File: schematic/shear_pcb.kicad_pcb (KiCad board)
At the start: 2 copper layers, 53.3 x 66 mm, 3 parts, among them U1 Teensy3.5, U2 AMIS30542, U3 AMIS30542

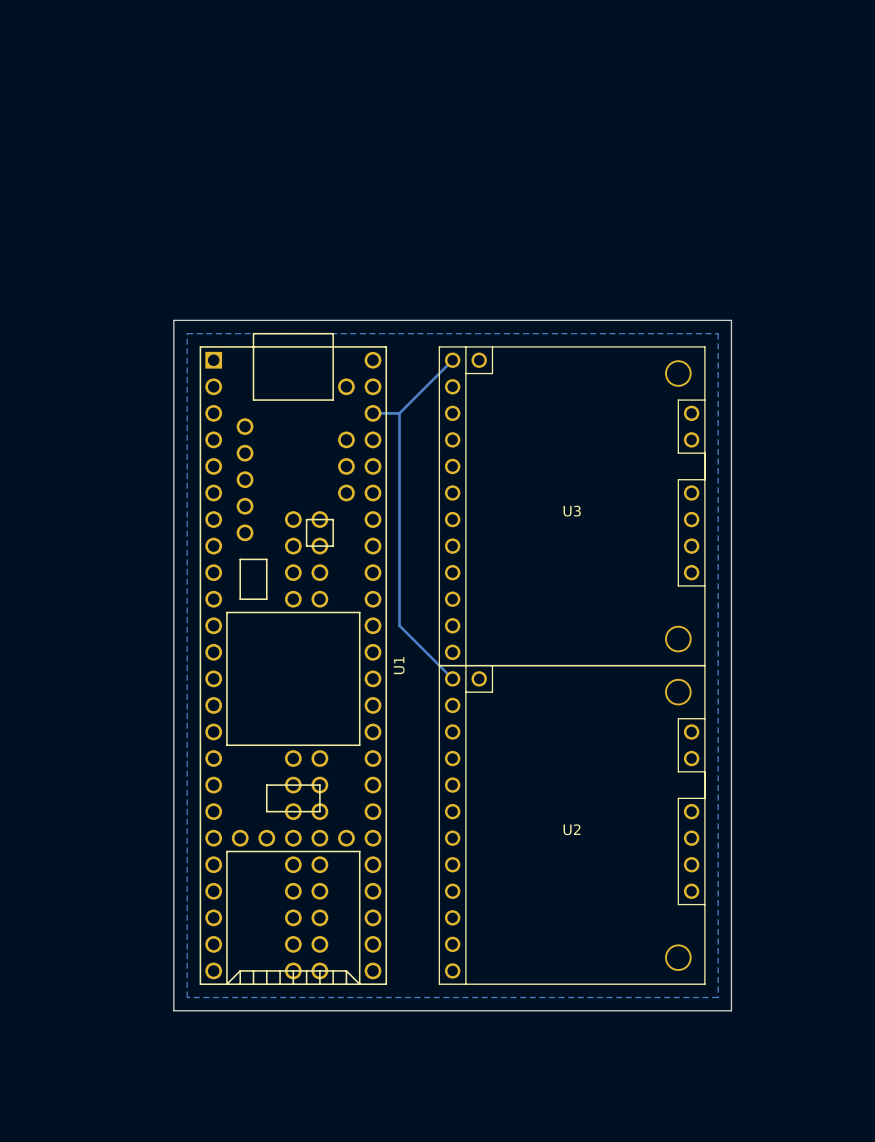
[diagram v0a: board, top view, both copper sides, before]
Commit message: Add connectors and first pcb design
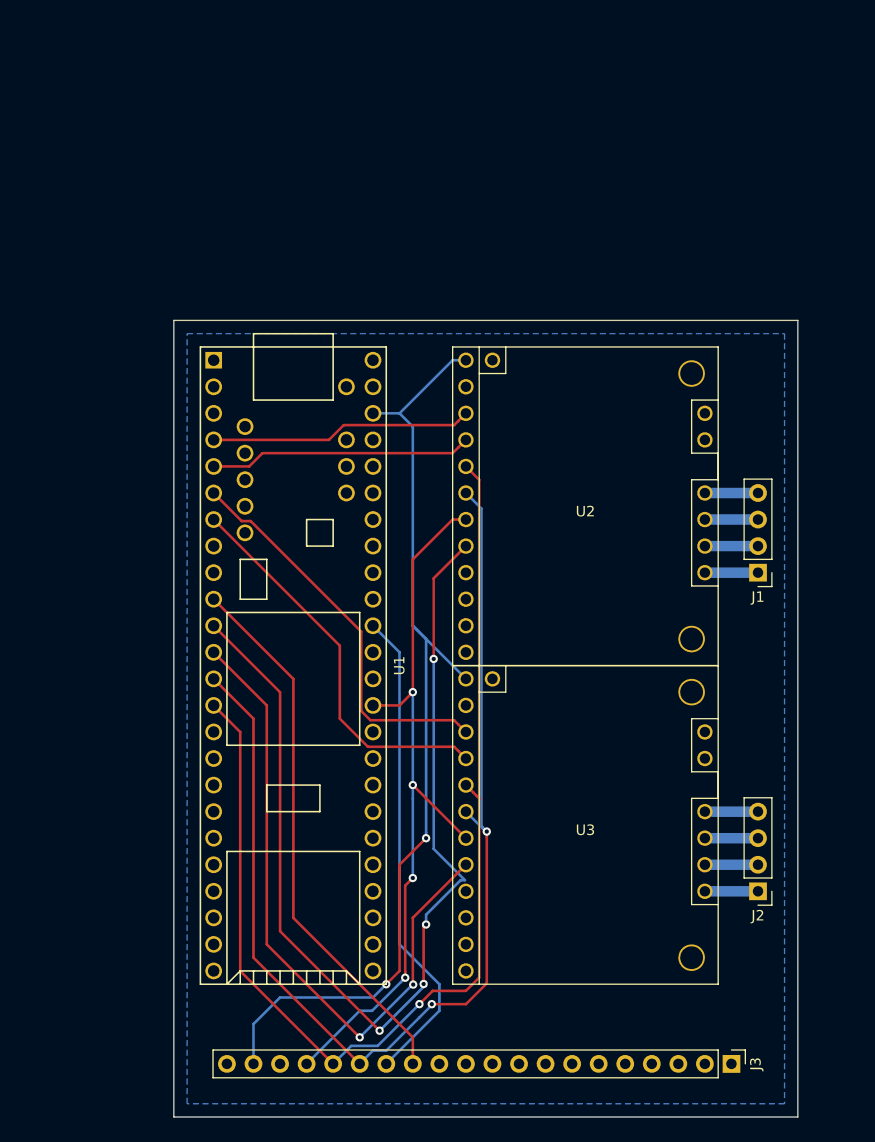
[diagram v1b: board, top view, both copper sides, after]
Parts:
- added J1: MOTOR1, Connector_PinHeader_2.54mm:PinHeader_1x04_P2.54mm_Vertical, F.Cu at (189.2, 97.8)
- added J2: MOTOR2, Connector_PinHeader_2.54mm:PinHeader_1x04_P2.54mm_Vertical, F.Cu at (189.2, 128.3)
- added J3: LCD_CONN, Connector_PinHeader_2.54mm:PinHeader_1x20_P2.54mm_Vertical, F.Cu at (186.7, 144.8)
- moved U2 30.5 mm to (172.7, 91.4)
- moved U3 30.5 mm to (172.7, 121.9)
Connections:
- U1 pad 10: Net-(U1-Pad10) -> D\C
- U1 pad 11: Net-(U1-Pad11) -> CS1
- U1 pad 12: Net-(U1-Pad12) -> CS2
- U1 pad 13: Net-(U1-Pad13) -> MOSI
- U1 pad 14: Net-(U1-Pad14) -> MISO
- U1 pad 4: Net-(U1-Pad4) -> STEP1
- U1 pad 40: Net-(U1-Pad40) -> CLK
- U1 pad 43: Net-(U1-Pad43) -> CS3
- U1 pad 5: Net-(U1-Pad5) -> DIR1
- U1 pad 6: Net-(U1-Pad6) -> STEP2
- U1 pad 7: Net-(U1-Pad7) -> DIR2
- U2 pad 14: GND -> Net-(U2-Pad14)
- U2 pad 15: Net-(U2-Pad15) -> GND
- U2 pad 19: (no net) -> Net-(J1-Pad1)
- U2 pad 4: Net-(U2-Pad4) -> STEP1
- U2 pad 5: Net-(U2-Pad5) -> DIR1
- U2 pad 6: Net-(U2-Pad6) -> MISO
- U2 pad 7: Net-(U2-Pad7) -> MOSI
- U2 pad 8: Net-(U2-Pad8) -> CLK
- U2 pad 9: Net-(U2-Pad9) -> CS1
- U3 pad 14: GND -> Net-(U3-Pad14)
- U3 pad 15: Net-(U3-Pad15) -> GND
- U3 pad 19: (no net) -> Net-(J2-Pad1)
- U3 pad 4: Net-(U3-Pad4) -> STEP2
- U3 pad 5: Net-(U3-Pad5) -> DIR2
- U3 pad 6: Net-(U3-Pad6) -> MISO
- U3 pad 7: Net-(U3-Pad7) -> MOSI
- U3 pad 8: Net-(U3-Pad8) -> CLK
- U3 pad 9: Net-(U3-Pad9) -> CS2
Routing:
- net MOSI: track 0.00 -> 108.5 mm, vias 0 -> 2
- net MISO: track 0.00 -> 107.6 mm, vias 0 -> 1
- net CS1: track 0.00 -> 97.8 mm, vias 0 -> 4
- net CLK: track 0.00 -> 71.3 mm, vias 0 -> 4
- net CS2: track 0.00 -> 63.4 mm, vias 0 -> 2
- net +3V3: track 37.2 -> 93.5 mm, vias 0 -> 2
- net D\C: track 0.00 -> 52.3 mm
- net CS3: track 0.00 -> 46.6 mm
- net STEP2: track 0.00 -> 38.1 mm
- net DIR2: track 0.00 -> 37.7 mm
- net STEP1: track 0.00 -> 25.2 mm
- net DIR1: track 0.00 -> 25.2 mm
- net Net-(J2-Pad4): track 0.00 -> 5.08 mm
- net Net-(J2-Pad3): track 0.00 -> 5.08 mm
- net Net-(J2-Pad2): track 0.00 -> 5.08 mm
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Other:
- board size 53.3 x 66 mm -> 59.7 x 76.2 mm
- net class Motor added: clearance 0.2, trace_width 1, via_dia 0.8, via_drill 0.4

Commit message: Redesign PCB for single-side fabrication
-Add power and endstop connectors
-Add LCD connector
-Reroute SPI and step/dir tracks
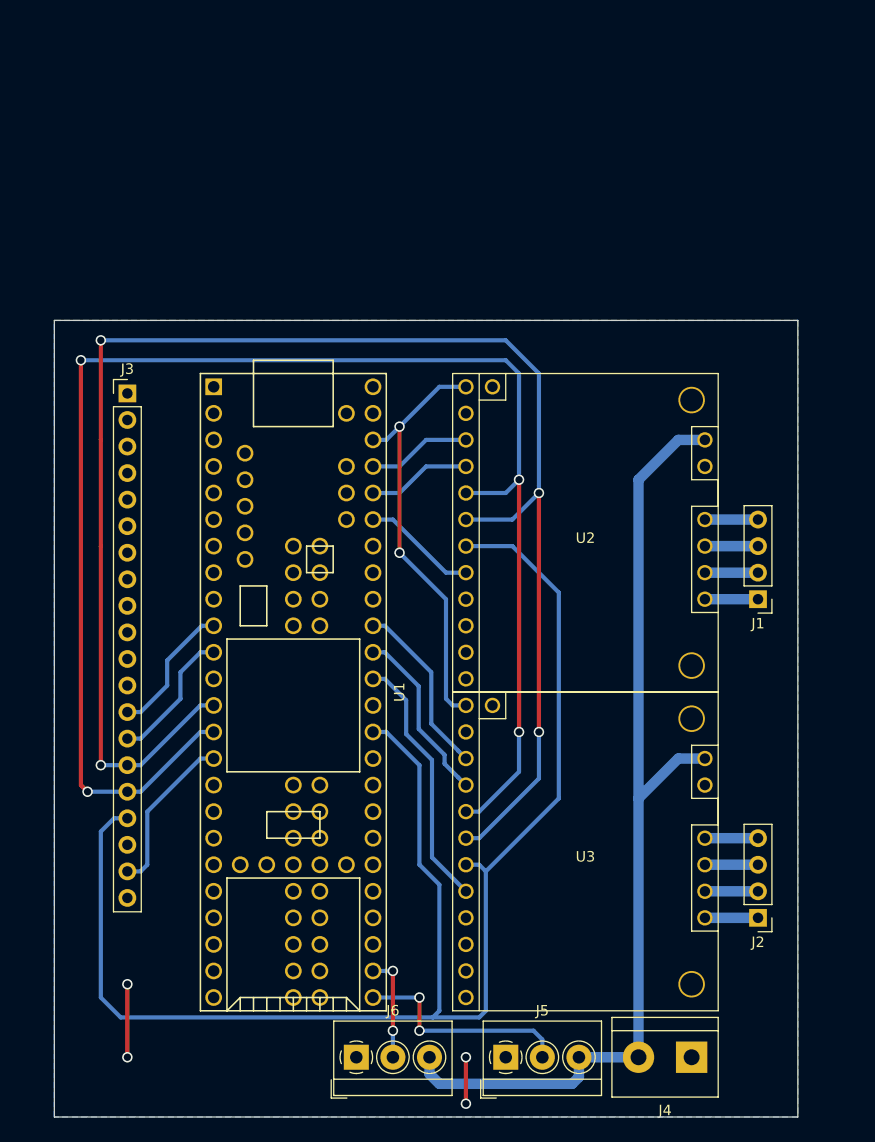
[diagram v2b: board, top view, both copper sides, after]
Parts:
- added J4: VIN, TerminalBlock:TerminalBlock_bornier-2_P5.08mm, F.Cu at (182.9, 144.1)
- added J5: ENDSTOP1, TerminalBlock_4Ucon:TerminalBlock_4Ucon_1x03_P3.50mm_Horizontal, F.Cu at (165.1, 144.1)
- added J6: ENDSTOP2, TerminalBlock_4Ucon:TerminalBlock_4Ucon_1x03_P3.50mm_Horizontal, F.Cu at (150.8, 144.1)
- moved J3 86.3 mm to (128.9, 80.6), turned to 0 degrees
- moved U2 2.54 mm to (172.7, 94.0)
- moved J1 2.54 mm to (189.2, 100.3)
- moved J2 2.54 mm to (189.2, 130.8)
- moved U1 2.54 mm to (144.8, 109.2)
- moved U3 2.54 mm to (172.7, 124.5)
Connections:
- J3 pad 1: Net-(J3-Pad1) -> (no net)
- J3 pad 10: YP -> (no net)
- J3 pad 11: Net-(J3-Pad11) -> (no net)
- J3 pad 12: Net-(J3-Pad12) -> (no net)
- J3 pad 14: CS3 -> CS1
- J3 pad 18: Net-(J3-Pad18) -> (no net)
- J3 pad 2: Net-(J3-Pad2) -> (no net)
- J3 pad 3: Net-(J3-Pad3) -> (no net)
- J3 pad 4: Net-(J3-Pad4) -> (no net)
- J3 pad 5: Net-(J3-Pad5) -> (no net)
- J3 pad 6: Net-(J3-Pad6) -> (no net)
- J3 pad 7: XM -> (no net)
- J3 pad 8: YM -> (no net)
- J3 pad 9: XP -> (no net)
- U1 pad 12: CS2 -> (no net)
- U1 pad 15: Net-(U1-Pad15) -> +3V3
- U1 pad 16: Net-(U1-Pad16) -> (no net)
- U1 pad 17: Net-(U1-Pad17) -> (no net)
- U1 pad 18: Net-(U1-Pad18) -> (no net)
- U1 pad 19: Net-(U1-Pad19) -> (no net)
- U1 pad 2: Net-(U1-Pad2) -> (no net)
- U1 pad 20: Net-(U1-Pad20) -> (no net)
- U1 pad 21: Net-(U1-Pad21) -> (no net)
- U1 pad 22: Net-(U1-Pad22) -> (no net)
- U1 pad 23: Net-(U1-Pad23) -> (no net)
- U1 pad 24: Net-(U1-Pad24) -> (no net)
- U1 pad 3: Net-(U1-Pad3) -> (no net)
- U1 pad 30: Net-(U1-Pad30) -> END1
- U1 pad 31: Net-(U1-Pad31) -> END2
- U1 pad 32: Net-(U1-Pad32) -> (no net)
- U1 pad 33: Net-(U1-Pad33) -> (no net)
- U1 pad 34: Net-(U1-Pad34) -> (no net)
- U1 pad 35: Net-(U1-Pad35) -> (no net)
- U1 pad 36: Net-(U1-Pad36) -> (no net)
- U1 pad 37: Net-(U1-Pad37) -> (no net)
- U1 pad 38: Net-(U1-Pad38) -> (no net)
- U1 pad 39: Net-(U1-Pad39) -> (no net)
- U1 pad 4: STEP1 -> (no net)
- U1 pad 41: Net-(U1-Pad41) -> (no net)
- U1 pad 42: Net-(U1-Pad42) -> CS2
- U1 pad 43: CS3 -> DIR2
- U1 pad 44: Net-(U1-Pad44) -> STEP2
- U1 pad 45: Net-(U1-Pad45) -> (no net)
- U1 pad 46: Net-(U1-Pad46) -> (no net)
- U1 pad 47: Net-(U1-Pad47) -> (no net)
- U1 pad 48: Net-(U1-Pad48) -> CS3
- U1 pad 49: Net-(U1-Pad49) -> DIR1
- U1 pad 5: DIR1 -> (no net)
- U1 pad 50: Net-(U1-Pad50) -> STEP1
- U1 pad 52: Net-(U1-Pad52) -> (no net)
- U1 pad 53: Net-(U1-Pad53) -> (no net)
- U1 pad 54: Net-(U1-Pad54) -> (no net)
- U1 pad 55: Net-(U1-Pad55) -> (no net)
- U1 pad 56: Net-(U1-Pad56) -> (no net)
- U1 pad 57: Net-(U1-Pad57) -> (no net)
- U1 pad 58: Net-(U1-Pad58) -> (no net)
- U1 pad 59: Net-(U1-Pad59) -> (no net)
- U1 pad 6: STEP2 -> (no net)
- U1 pad 60: Net-(U1-Pad60) -> (no net)
- U1 pad 61: Net-(U1-Pad61) -> (no net)
- U1 pad 62: Net-(U1-Pad62) -> (no net)
- U1 pad 7: DIR2 -> (no net)
- U1 pad 8: Net-(U1-Pad8) -> (no net)
- U1 pad 9: Net-(U1-Pad9) -> (no net)
- U2 pad 1: Net-(U2-Pad1) -> (no net)
- U2 pad 10: Net-(U2-Pad10) -> (no net)
- U2 pad 11: Net-(U2-Pad11) -> (no net)
- U2 pad 12: Net-(U2-Pad12) -> (no net)
- U2 pad 13: Net-(U2-Pad13) -> (no net)
- U2 pad 14: Net-(U2-Pad14) -> VDC
- U2 pad 3: Net-(U2-Pad3) -> (no net)
- U2 pad 9: CS1 -> CS3
- U3 pad 1: Net-(U3-Pad1) -> (no net)
- U3 pad 10: Net-(U3-Pad10) -> (no net)
- U3 pad 11: Net-(U3-Pad11) -> (no net)
- U3 pad 12: Net-(U3-Pad12) -> (no net)
- U3 pad 13: Net-(U3-Pad13) -> (no net)
- U3 pad 14: Net-(U3-Pad14) -> VDC
- U3 pad 3: Net-(U3-Pad3) -> (no net)
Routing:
- net VDC: track 0.00 -> 95.2 mm
- net CS1: track 97.8 -> 13.2 mm, vias 4 -> 0
- net CLK: track 71.3 -> 143.6 mm, vias 4 -> 0
- net MOSI: track 108.5 -> 153.2 mm, vias 2 -> 4
- net MISO: track 107.6 -> 148.8 mm, vias 1 -> 4
- net D\C: track 52.3 -> 13.1 mm
- net CS2: track 63.4 -> 24.7 mm, vias 2 -> 0
- net +3V3: track 93.5 -> 56.7 mm
- net CS3: track 46.6 -> 11.0 mm
- net END1: track 0.00 -> 21.9 mm, vias 0 -> 2
- net STEP2: track 38.1 -> 17.0 mm
- net DIR2: track 37.7 -> 17.0 mm
- net STEP1: track 25.2 -> 9.94 mm
- net DIR1: track 25.2 -> 9.94 mm
- net GND: track 0.00 -> 11.4 mm, vias 0 -> 4
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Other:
- board size 59.7 x 76.2 mm -> 71.1 x 76.2 mm
- net class Default: clearance 0.2 -> 0.8; trace_width 0.25 -> 0.4; via_dia 0.8 -> 1; via_drill 0.4 -> 0.7
- net class Motor: clearance 0.2 -> 0.8; via_dia 0.8 -> 1; via_drill 0.4 -> 0.7
- net class Power added: clearance 0.8, trace_width 1, via_dia 1, via_drill 0.7
- rule trace_clearance: 0.2 -> 0.8
- rule trace_min: 0.2 -> 0.4
- rule via_min_drill: 0.3 -> 0.7
- rule via_min_size: 0.4 -> 1

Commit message: Update repo in preparation for new computer
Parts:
- added R1: 4k7, Resistor_THT:R_Axial_DIN0204_L3.6mm_D1.6mm_P7.62mm_Horizontal, F.Cu at (156.8, 128.3)
- added R2: 4k7, Resistor_THT:R_Axial_DIN0204_L3.6mm_D1.6mm_P7.62mm_Horizontal, F.Cu at (138.4, 142.2)
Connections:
- J3 pad 1: (no net) -> Net-(J3-Pad1)
- J3 pad 10: (no net) -> YP
- J3 pad 11: (no net) -> Net-(J3-Pad11)
- J3 pad 12: (no net) -> Net-(J3-Pad12)
- J3 pad 18: (no net) -> Net-(J3-Pad18)
- J3 pad 2: (no net) -> Net-(J3-Pad2)
- J3 pad 3: (no net) -> Net-(J3-Pad3)
- J3 pad 4: (no net) -> Net-(J3-Pad4)
- J3 pad 5: (no net) -> Net-(J3-Pad5)
- J3 pad 6: (no net) -> Net-(J3-Pad6)
- J3 pad 7: (no net) -> XM
- J3 pad 8: (no net) -> YM
- J3 pad 9: (no net) -> XP
- U1 pad 12: (no net) -> Net-(U1-Pad12)
- U1 pad 16: (no net) -> Net-(U1-Pad16)
- U1 pad 17: (no net) -> Net-(U1-Pad17)
- U1 pad 18: (no net) -> Net-(U1-Pad18)
- U1 pad 19: (no net) -> Net-(U1-Pad19)
- U1 pad 2: (no net) -> Net-(U1-Pad2)
- U1 pad 20: (no net) -> Net-(U1-Pad20)
- U1 pad 21: (no net) -> Net-(U1-Pad21)
- U1 pad 22: (no net) -> Net-(U1-Pad22)
- U1 pad 23: (no net) -> YM
- U1 pad 24: (no net) -> XP
- U1 pad 25: (no net) -> Net-(U1-Pad25)
- U1 pad 26: (no net) -> Net-(U1-Pad26)
- U1 pad 27: (no net) -> Net-(U1-Pad27)
- U1 pad 28: (no net) -> Net-(U1-Pad28)
- U1 pad 29: (no net) -> Net-(U1-Pad29)
- U1 pad 3: (no net) -> Net-(U1-Pad3)
- U1 pad 32: (no net) -> Net-(U1-Pad32)
- U1 pad 33: (no net) -> Net-(U1-Pad33)
- U1 pad 34: (no net) -> Net-(U1-Pad34)
- U1 pad 35: (no net) -> Net-(U1-Pad35)
- U1 pad 36: (no net) -> Net-(U1-Pad36)
- U1 pad 37: (no net) -> Net-(U1-Pad37)
- U1 pad 38: (no net) -> Net-(U1-Pad38)
- U1 pad 39: (no net) -> Net-(U1-Pad39)
- U1 pad 4: (no net) -> Net-(U1-Pad4)
- U1 pad 41: (no net) -> Net-(U1-Pad41)
- U1 pad 45: (no net) -> Net-(U1-Pad45)
- U1 pad 46: (no net) -> Net-(U1-Pad46)
- U1 pad 47: (no net) -> Net-(U1-Pad47)
- U1 pad 5: (no net) -> Net-(U1-Pad5)
- U1 pad 52: (no net) -> Net-(U1-Pad52)
- U1 pad 53: (no net) -> Net-(U1-Pad53)
- U1 pad 54: (no net) -> Net-(U1-Pad54)
- U1 pad 55: (no net) -> Net-(U1-Pad55)
- U1 pad 56: (no net) -> Net-(U1-Pad56)
- U1 pad 57: (no net) -> Net-(U1-Pad57)
- U1 pad 58: (no net) -> Net-(U1-Pad58)
- U1 pad 59: (no net) -> Net-(U1-Pad59)
- U1 pad 6: (no net) -> Net-(U1-Pad6)
- U1 pad 60: (no net) -> Net-(U1-Pad60)
- U1 pad 61: (no net) -> Net-(U1-Pad61)
- U1 pad 62: (no net) -> Net-(U1-Pad62)
- U1 pad 63: (no net) -> Net-(U1-Pad63)
- U1 pad 64: (no net) -> Net-(U1-Pad64)
- U1 pad 65: (no net) -> Net-(U1-Pad65)
- U1 pad 66: (no net) -> Net-(U1-Pad66)
- U1 pad 67: (no net) -> Net-(U1-Pad67)
- U1 pad 68: (no net) -> Net-(U1-Pad68)
- U1 pad 69: (no net) -> Net-(U1-Pad69)
- U1 pad 7: (no net) -> XM
- U1 pad 70: (no net) -> Net-(U1-Pad70)
- U1 pad 71: (no net) -> Net-(U1-Pad71)
- U1 pad 72: (no net) -> Net-(U1-Pad72)
- U1 pad 73: (no net) -> Net-(U1-Pad73)
- U1 pad 74: (no net) -> Net-(U1-Pad74)
- U1 pad 75: (no net) -> Net-(U1-Pad75)
- U1 pad 76: (no net) -> Net-(U1-Pad76)
- U1 pad 77: (no net) -> Net-(U1-Pad77)
- U1 pad 78: (no net) -> Net-(U1-Pad78)
- U1 pad 79: (no net) -> Net-(U1-Pad79)
- U1 pad 8: (no net) -> Net-(U1-Pad8)
- U1 pad 80: (no net) -> Net-(U1-Pad80)
- U1 pad 81: (no net) -> Net-(U1-Pad81)
- U1 pad 82: (no net) -> Net-(U1-Pad82)
- U1 pad 83: (no net) -> Net-(U1-Pad83)
- U1 pad 84: (no net) -> Net-(U1-Pad84)
- U1 pad 85: (no net) -> Net-(U1-Pad85)
- U1 pad 86: (no net) -> Net-(U1-Pad86)
- U1 pad 9: (no net) -> YP
- U2 pad 1: (no net) -> Net-(U2-Pad1)
- U2 pad 10: (no net) -> Net-(U2-Pad10)
- U2 pad 11: (no net) -> Net-(U2-Pad11)
- U2 pad 12: (no net) -> Net-(U2-Pad12)
- U2 pad 13: (no net) -> Net-(U2-Pad13)
- U2 pad 3: (no net) -> Net-(U2-Pad3)
- U3 pad 1: (no net) -> Net-(U3-Pad1)
- U3 pad 10: (no net) -> Net-(U3-Pad10)
- U3 pad 11: (no net) -> Net-(U3-Pad11)
- U3 pad 12: (no net) -> Net-(U3-Pad12)
- U3 pad 13: (no net) -> Net-(U3-Pad13)
- U3 pad 3: (no net) -> Net-(U3-Pad3)
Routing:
- net +3V3: track 56.7 -> 114.4 mm, vias 2 -> 5
- net YM: track 0.00 -> 45.7 mm, vias 0 -> 2
- net XP: track 0.00 -> 45.6 mm, vias 0 -> 2
- net YP: track 0.00 -> 9.57 mm
- net END2: track 10.2 -> 18.8 mm
- net XM: track 0.00 -> 8.52 mm
- net END1: track 21.9 -> 24.3 mm
